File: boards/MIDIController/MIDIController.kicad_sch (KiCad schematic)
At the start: 15 parts, among them J1 Ctrl, J4 USB_A, J5 I2S_Data, J6 I2C_Pwr, J7 Raspberry_Pi_2_3, J8 RJ45_Amphenol_RJMG1BD3B8K1ANR, U1 Teensy4.1

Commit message: Added CR2032 holder footprint, allow routing between pins
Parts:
- BT1: footprint (none) -> Custom_Footprints:BatteryHolder_Holder_CR2032
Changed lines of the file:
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@@
 			)
 		)
-		(property "Footprint" ""
+		(property "Footprint" "Custom_Footprints:BatteryHolder_Holder_CR2032"
 			(at 90.17 131.826 90)
 			(effects

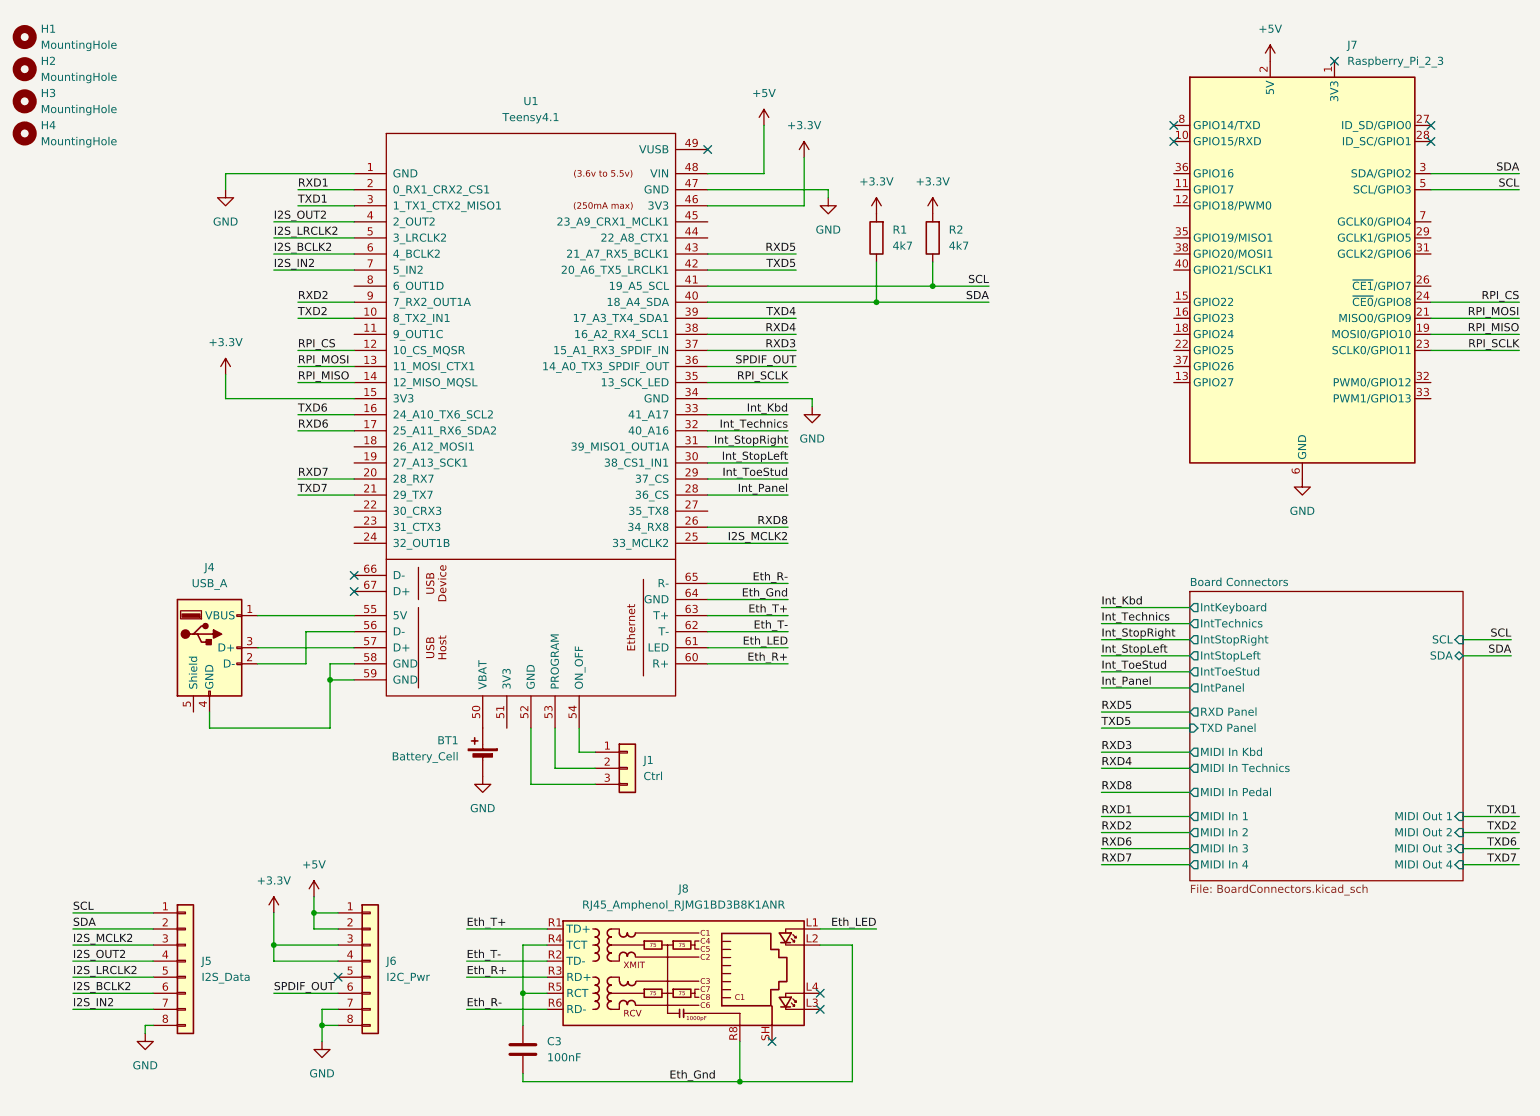
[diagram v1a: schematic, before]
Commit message: Updated design rules to 0.32mm template and exported Gerber files
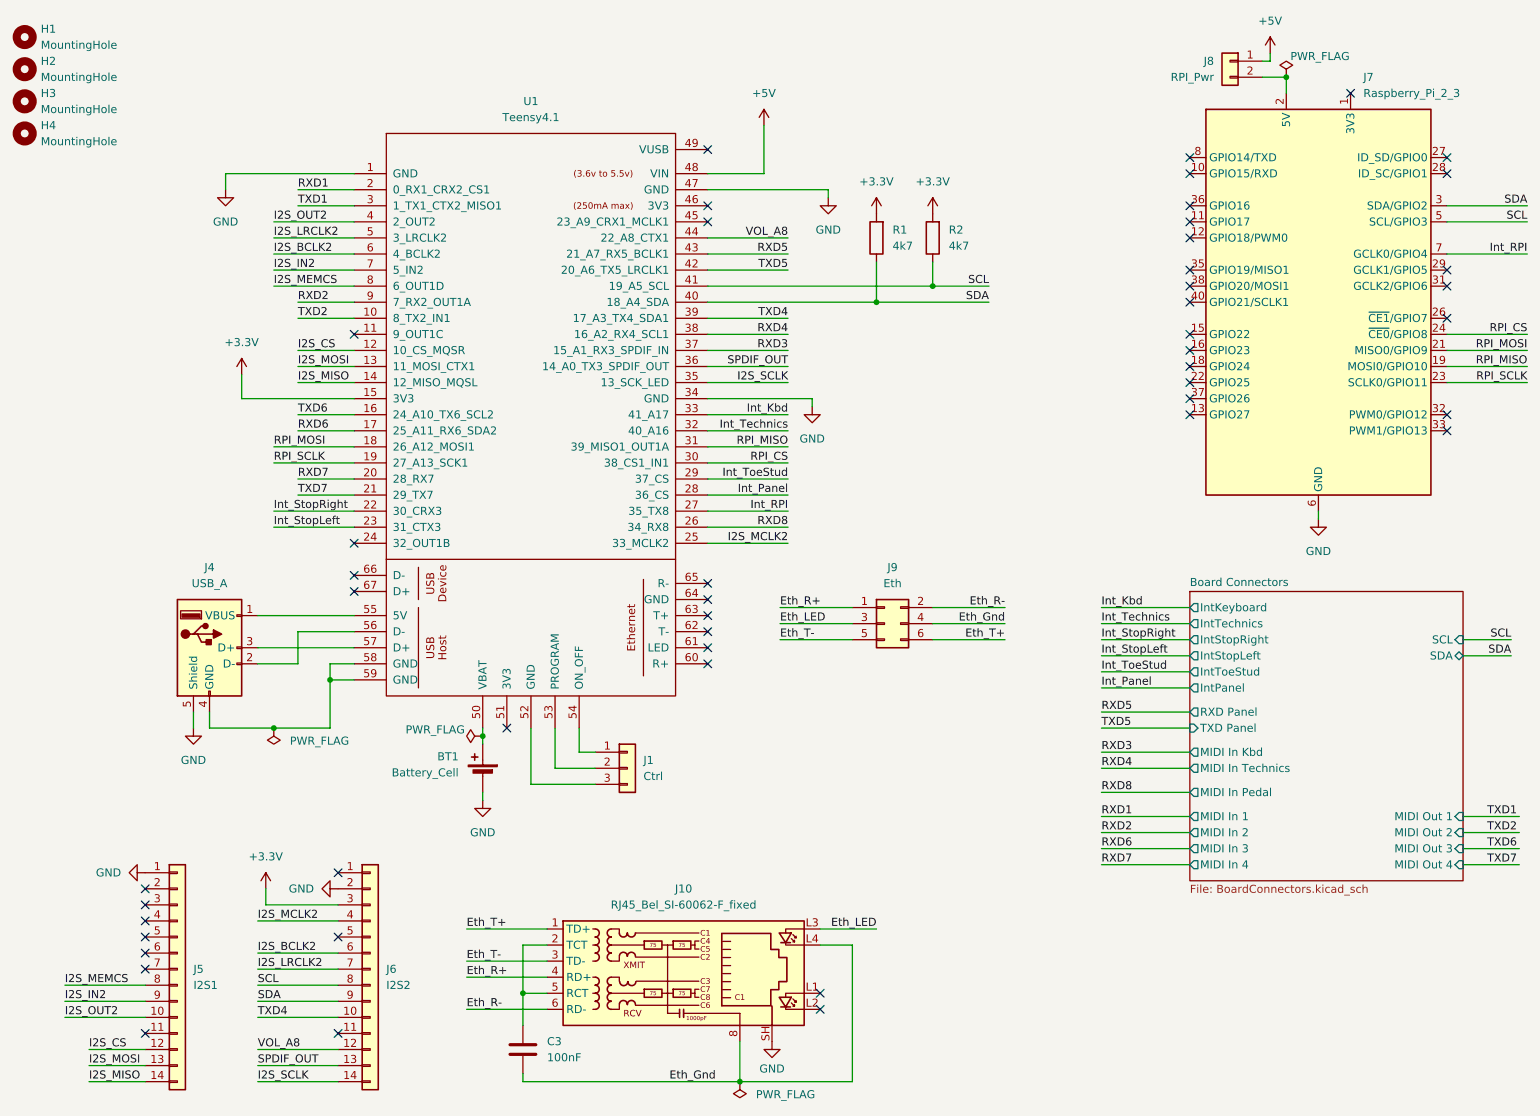
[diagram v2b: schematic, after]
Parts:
- removed J5: I2S_Data, Connector_PinHeader_2.54mm:PinHeader_1x08_P2.54mm_Vertical, symbol Connector_Generic:Conn_01x08
- removed J6: I2C_Pwr, Connector_PinHeader_2.54mm:PinHeader_1x08_P2.54mm_Vertical, symbol Connector_Generic:Conn_01x08
- removed J8: RJ45_Amphenol_RJMG1BD3B8K1ANR, Connector_RJ:RJ45_Amphenol_RJMG1BD3B8K1ANR, symbol Connector:RJ45_Amphenol_RJMG1BD3B8K1ANR
- removed U1: Teensy4.1, Teensy:Teensy41, symbol Teensy:Teensy4.1
- added J10: RJ45_Bel_SI-60062-F_fixed, Connector_RJ:RJ45_Bel_SI-60062-F, symbol Custom_Symbols:RJ45_Bel_SI-60062-F_fixed
- added J5: I2S1, Connector_PinHeader_2.54mm:PinHeader_1x14_P2.54mm_Vertical, symbol Connector_Generic:Conn_01x14
- added J6: I2S2, Connector_PinHeader_2.54mm:PinHeader_1x14_P2.54mm_Vertical, symbol Connector_Generic:Conn_01x14
- added J8: RPI_Pwr, Connector_PinHeader_2.54mm:PinHeader_1x02_P2.54mm_Vertical, symbol Connector_Generic:Conn_01x02
- added J9: Eth, Connector_PinHeader_2.00mm:PinHeader_2x03_P2.00mm_Vertical, symbol Connector_Generic:Conn_02x03_Odd_Even
- added U1: Teensy4.1, teensy:Teensy41, symbol teensy:Teensy4.1
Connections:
- net +3.3V: now also J6.3 (Pin_3), U1.15 (3V3)
- net +5V: now also J8.1 (Pin_1), U1.48 (VIN); no longer J7.2 (5V), J7.4 (5V)
- net Eth_Gnd: now also J10.8, J10.L4, J9.4 (Pin_4)
- net Eth_LED: now also J10.L3, J9.3 (Pin_3)
- net Eth_R+: now also J10.4 (RD+), J9.1 (Pin_1)
- net Eth_R-: now also J10.6 (RD-), J9.2 (Pin_2)
- net Eth_T+: now also J10.1 (TD+), J9.6 (Pin_6)
- net Eth_T-: now also J10.3 (TD-), J9.5 (Pin_5)
- net GND: now also J4.5 (Shield), J10.SH, J5.1 (Pin_1), J6.2 (Pin_2), U1.1 (GND), U1.34 (GND), U1.47 (GND)
- net I2S_BCLK2: now also J6.6 (Pin_6), U1.6 (4_BCLK2)
- net I2S_IN2: now also J5.9 (Pin_9), U1.7 (5_IN2)
- net I2S_LRCLK2: now also J6.7 (Pin_7), U1.5 (3_LRCLK2)
- net I2S_MCLK2: now also J6.4 (Pin_4), U1.25 (33_MCLK2)
- net I2S_OUT2: now also J5.10 (Pin_10), U1.4 (2_OUT2)
- net Int_Kbd: now also U1.33 (41_A17)
- net Int_Panel: now also U1.28 (36_CS)
- net Int_StopLeft: now also U1.23 (31_CTX3)
- net Int_StopRight: now also U1.22 (30_CRX3)
- net Int_Technics: now also U1.32 (40_A16)
- net Int_ToeStud: now also U1.29 (37_CS)
- net RPI_CS: now also U1.30 (38_CS1_IN1)
- net RPI_MISO: now also U1.31 (39_MISO1_OUT1A)
- net RPI_MOSI: now also U1.18 (26_A12_MOSI1)
- net RPI_SCLK: now also U1.19 (27_A13_SCK1)
- net RXD1: now also U1.2 (0_RX1_CRX2_CS1)
- net RXD2: now also U1.9 (7_RX2_OUT1A)
- net RXD3: now also U1.37 (15_A1_RX3_SPDIF_IN)
- net RXD4: now also U1.38 (16_A2_RX4_SCL1)
- net RXD5: now also U1.43 (21_A7_RX5_BCLK1)
- net RXD6: now also U1.17 (25_A11_RX6_SDA2)
- net RXD7: now also U1.20 (28_RX7)
- net RXD8: now also U1.26 (34_RX8)
- net SCL: now also J6.8 (Pin_8), U1.41 (19_A5_SCL)
- net SDA: now also J6.9 (Pin_9), U1.40 (18_A4_SDA)
- net SPDIF_OUT: now also J6.13 (Pin_13), U1.36 (14_A0_TX3_SPDIF_OUT)
- net TXD1: now also U1.3 (1_TX1_CTX2_MISO1)
- net TXD2: now also U1.10 (8_TX2_IN1)
- net TXD4: now also J6.10 (Pin_10), U1.39 (17_A3_TX4_SDA1)
- net TXD5: now also U1.42 (20_A6_TX5_LRCLK1)
- net TXD6: now also U1.16 (24_A10_TX6_SCL2)
- net TXD7: now also U1.21 (29_TX7)
- net at J4.1 (VBUS): now also U1.55 (5V)
- net at J4.2 (D-): now also U1.56 (D-)
- net at J4.3 (D+): now also U1.57 (D+)
- net at J4.4 (GND): now also U1.58 (GND), U1.59 (GND)
- net at C3.1: now also J10.2 (TCT), J10.5 (RCT)
- net Int_RPI: now reaches J7.7 (GCLK0/GPIO4)
- net Int_RPI: now also U1.27 (35_TX8)
- net at BT1.1 (+): now also U1.50 (VBAT)
- net at J1.3 (Pin_3): now also U1.52 (GND)
- net at J1.2 (Pin_2): now also U1.53 (PROGRAM)
- net at J1.1 (Pin_1): now also U1.54 (ON_OFF)
- new net: J7.2 (5V), J7.4 (5V), J8.2 (Pin_2)
- new net I2S_CS: J5.12 (Pin_12), U1.12 (10_CS_MQSR)
- new net I2S_MEMCS: J5.8 (Pin_8), U1.8 (6_OUT1D)
- new net I2S_MISO: J5.14 (Pin_14), U1.14 (12_MISO_MQSL)
- new net I2S_MOSI: J5.13 (Pin_13), U1.13 (11_MOSI_CTX1)
- new net I2S_SCLK: J6.14 (Pin_14), U1.35 (13_SCK_LED)
- new net VOL_A8: J6.12 (Pin_12), U1.44 (22_A8_CTX1)
- no-connect marks 12 -> 48
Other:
- moved on the sheet: BT1, J7

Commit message: Fixed some RX/TX pin swaps
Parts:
- removed J1: Ctrl, Connector_PinHeader_2.54mm:PinHeader_1x03_P2.54mm_Vertical, symbol Connector_Generic:Conn_01x03
- added H5, H6, H7: MountingHole, MountingHole:MountingHole_2.7mm_M2.5, symbol Mechanical:MountingHole
- added J1: VBAT, Connector_PinHeader_2.54mm:PinHeader_1x01_P2.54mm_Vertical, symbol Connector_Generic:Conn_01x01
- added J11: USB, Connector_PinHeader_2.54mm:PinHeader_1x04_P2.54mm_Vertical, symbol Connector_Generic:Conn_01x04
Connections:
- net +3.3V: no longer R1.2, R2.2
- net Int_Kbd: now also U1.24 (32_OUT1B); no longer U1.33 (41_A17)
- net Int_RPI: now also U1.29 (37_CS); no longer U1.27 (35_TX8)
- net Int_StopLeft: now also U1.32 (40_A16); no longer U1.23 (31_CTX3)
- net Int_StopRight: now also U1.33 (41_A17); no longer U1.22 (30_CRX3)
- net Int_Technics: now also U1.23 (31_CTX3); no longer U1.32 (40_A16)
- net Int_ToeStud: now also U1.22 (30_CRX3); no longer U1.29 (37_CS)
- net TXD2: now also J6.10 (Pin_10)
- net TXD4: no longer J6.10 (Pin_10)
- net at J4.1 (VBUS): now also J11.1 (Pin_1); no longer U1.55 (5V)
- net at J4.2 (D-): now also J11.2 (Pin_2); no longer U1.56 (D-)
- net at J4.3 (D+): now also J11.3 (Pin_3); no longer U1.57 (D+)
- net +3.3V': now reaches U1.46 (3V3)
- net +3.3V': now also R1.2, R2.2
- net at U1.50 (VBAT): no longer BT1.1 (+)
- new net: J11.4 (Pin_4), J4.4 (GND)
- new net: BT1.1 (+), J1.1 (Pin_1)
- now unconnected: U1.58 (GND), U1.59 (GND)
- no-connect marks 48 -> 56
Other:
- moved on the sheet: BT1, C3, J10, J4

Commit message: Fixed mirrored MIDI board connector
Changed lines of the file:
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@@
 	)
 	(label "RXD7"
-		(at 187.96 142.24 0)
+		(at 187.96 147.32 0)
 		(fields_autoplaced yes)
 		(effects
@@
 	)
 	(label "RXD5"
-		(at 187.96 147.32 0)
+		(at 187.96 142.24 0)
 		(fields_autoplaced yes)
 		(effects
@@
 	)
 	(label "TXD7"
-		(at 254 142.24 180)
+		(at 254 147.32 180)
 		(fields_autoplaced yes)
 		(effects
@@
 	)
 	(label "TXD5"
-		(at 254 147.32 180)
-		(fields_autoplaced yes)
-		(effects
+		(at 254 142.24 180)
+		(fields_autoplaced yes)
+		(effects

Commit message: Fixed swapped I2S data lines in schematics
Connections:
- net I2S_IN2: now also J5.10 (Pin_10); no longer J5.9 (Pin_9)
- net I2S_OUT2: now also J5.9 (Pin_9); no longer J5.10 (Pin_10)
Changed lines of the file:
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@@
 	)
 	(label "I2S_IN2"
-		(at 24.13 171.45 0)
+		(at 24.13 173.99 0)
 		(fields_autoplaced yes)
 		(effects
@@
 	)
 	(label "I2S_OUT2"
-		(at 24.13 173.99 0)
-		(fields_autoplaced yes)
-		(effects
+		(at 24.13 171.45 0)
+		(fields_autoplaced yes)
+		(effects

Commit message: Fixed MIDIController I2S PCB, added LED
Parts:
- removed J1: VBAT, Connector_PinHeader_2.54mm:PinHeader_1x01_P2.54mm_Vertical, symbol Connector_Generic:Conn_01x01
- added D1: LED, LED_THT:LED_D3.0mm, symbol Device:LED
- added J1: Bat, Connector_PinHeader_2.54mm:PinHeader_1x02_P2.54mm_Vertical, symbol Connector_Generic:Conn_01x02
- added R9: 470, Resistor_THT:R_Axial_DIN0207_L6.3mm_D2.5mm_P10.16mm_Horizontal, symbol Device:R
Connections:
- net GND: now also D1.1 (K), J1.1 (Pin_1)
- net LED: now reaches U1.45 (23_A9_CRX1_MCLK1)
- net LED: now also R9.2
- net at BT1.1 (+): now also J1.2 (Pin_2)
- new net: D1.2 (A), R9.1
- no-connect marks 56 -> 55

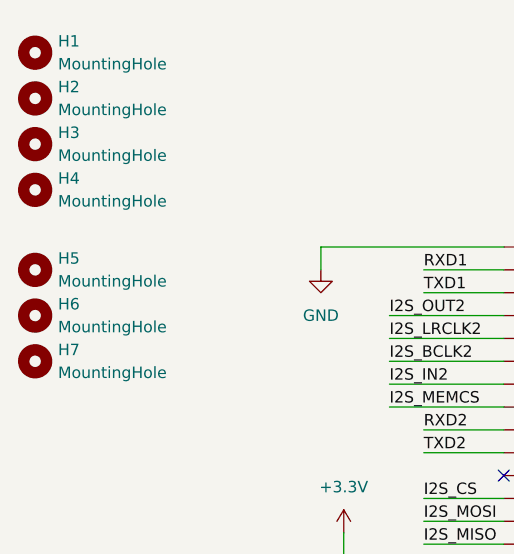
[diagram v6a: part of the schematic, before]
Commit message: Added line jacks for the audio board.
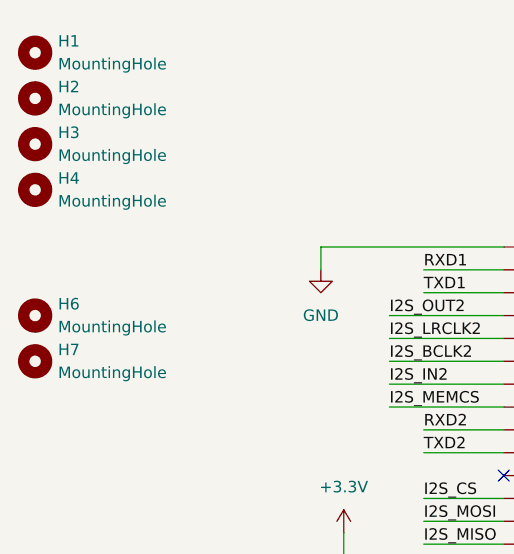
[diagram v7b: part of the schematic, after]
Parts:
- removed H5: MountingHole, MountingHole:MountingHole_2.7mm_M2.5, symbol Mechanical:MountingHole
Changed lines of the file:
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@@
-	)
-	(symbol
-		(lib_name "MountingHole_1")
-		(lib_id "Mechanical:MountingHole")
-		(at 17.78 43.18 0)
-		(unit 1)
-		(exclude_from_sim yes)
-		(in_bom no)
-		(on_board yes)
-		(dnp no)
-		(fields_autoplaced yes)
-		(property "Reference" "H5"
-			(at 20.32 41.9099 0)
-			(effects
-				(font
-					(size 1.27 1.27)
-				)
-				(justify left)
-			)
-		)
-		(property "Value" "MountingHole"
-			(at 20.32 44.4499 0)
-			(effects
-				(font
-					(size 1.27 1.27)
-				)
-				(justify left)
-			)
-		)
-		(property "Footprint" "MountingHole:MountingHole_2.7mm_M2.5"
-			(at 17.78 43.18 0)
-			(effects
-				(font
-					(size 1.27 1.27)
-				)
-				(hide yes)
-			)
-		)
-		(property "Datasheet" "~"
-			(at 17.78 43.18 0)
-			(effects
-				(font
-					(size 1.27 1.27)
-				)
-				(hide yes)
-			)
-		)
-		(property "Description" "Mounting Hole without connection"
-			(at 17.78 43.18 0)
-			(effects
-				(font
-					(size 1.27 1.27)
-				)
-				(hide yes)
-			)
-		)
-		(instances
-			(project "MIDIController"
-				(path "/92e30726-a111-410e-a189-3ef5a23983ec"
-					(reference "H5")
-					(unit 1)
-				)
-			)
-		)
 	)
 	(symbol
